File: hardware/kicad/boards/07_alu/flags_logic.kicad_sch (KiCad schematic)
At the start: 14 parts, among them U1 74AHC541, U16 74ACT151, U2 74HC00, U36 74HC86, U4 74HC688, U40 74LS377, U6 74HC00

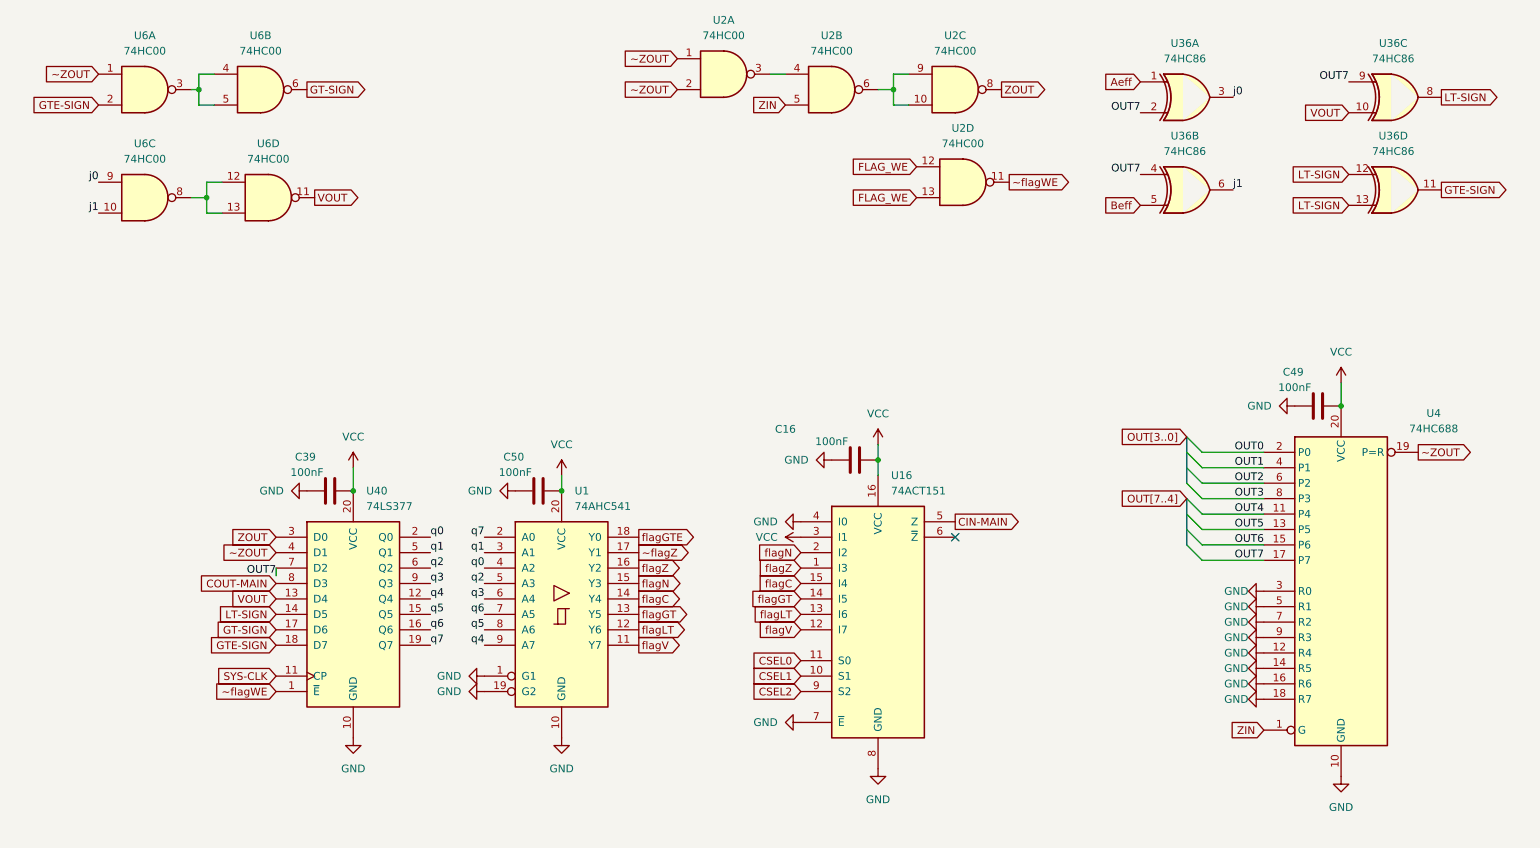
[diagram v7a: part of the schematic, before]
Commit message: feat: route 8b ALU slice and annotate pending final signoff 🎉🎉
Highlights:
- 0 ERC/DRC errors
- 0 Unrouted nets
- 2345 track segments
- 388 vias after cleanup
- 760 pads
- 18 core 74xx chips
- 7 flag 74xx chips

Pending additional confirmation of hardware-simulation faithfulness and fidelity.
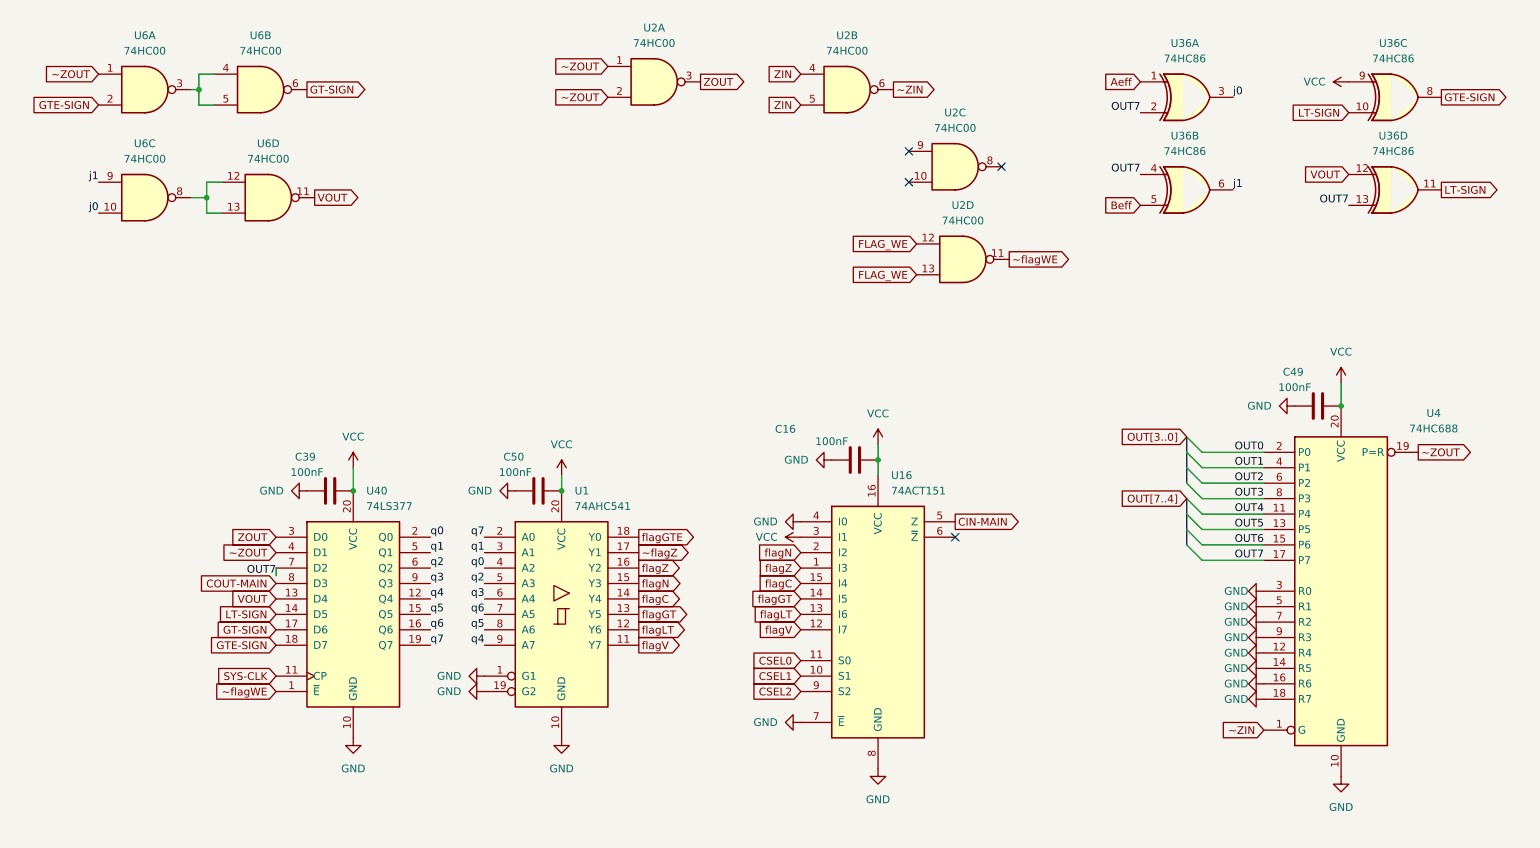
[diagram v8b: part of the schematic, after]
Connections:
- net GTE-SIGN: now also U36.8; no longer U36.11
- net LT-SIGN: now also U36.10, U36.11; no longer U36.12, U36.13, U36.8
- net OUT7: now also U36.13; no longer U36.9
- net VCC: now also U36.9
- net VOUT: now also U36.12; no longer U36.10
- net ZIN: now also U2.4; no longer U4.1 (G)
- net ZOUT: now also U2.3; no longer U2.8
- net j0: now also U6.10; no longer U6.9
- net j1: now also U6.9; no longer U6.10
- new net ~ZIN: U2.6, U4.1 (G)
- now unconnected: U2.10, U2.9
- no-connect marks 1 -> 4
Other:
- moved on the sheet: U2A, U2B, U2C, U2D
